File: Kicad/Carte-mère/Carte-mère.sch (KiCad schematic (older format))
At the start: 15 parts, among them P1 CONN_01X10, P2 CONN_01X04, P3 CONN_01X06, P4 CONN_01X06, P5 CONN_01X04, P6 CONN_01X04

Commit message: Mise à jour de la carte mère
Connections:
- net GND: now also ARD1.19 (GND), DRV1.15 (GND), DRV2.15 (GND)
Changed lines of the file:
@@
 Text Notes 5050 6350 0    60   ~ 0
 TX/RX communication
+$Comp
+L GND #PWR?
+U 1 1 55F57DDC
+P 5500 4700
+F 0 "#PWR?" H 5500 4700 30  0001 C CNN
+F 1 "GND" H 5500 4630 30  0001 C CNN
+F 2 "" H 5500 4700 60  0000 C CNN
+F 3 "" H 5500 4700 60  0000 C CNN
+	1    5500 4700
+	0    -1   -1   0
+$EndComp
+Wire Wire Line
+	5200 4700 5500 4700
+$Comp
+L GND #PWR?
+U 1 1 55F57EFC
+P 7950 4600
+F 0 "#PWR?" H 7950 4600 30  0001 C CNN
+F 1 "GND" H 7950 4530 30  0001 C CNN
+F 2 "" H 7950 4600 60  0000 C CNN
+F 3 "" H 7950 4600 60  0000 C CNN
+	1    7950 4600
+	0    -1   -1   0
+$EndComp
+Wire Wire Line
+	7750 4600 7950 4600
+$Comp
+L GND #PWR?
+U 1 1 55F57FF0
+P 7950 3550
+F 0 "#PWR?" H 7950 3550 30  0001 C CNN
+F 1 "GND" H 7950 3480 30  0001 C CNN
+F 2 "" H 7950 3550 60  0000 C CNN
+F 3 "" H 7950 3550 60  0000 C CNN
+	1    7950 3550
+	0    -1   -1   0
+$EndComp
+Wire Wire Line
+	7750 3550 7950 3550
 $EndSCHEMATC

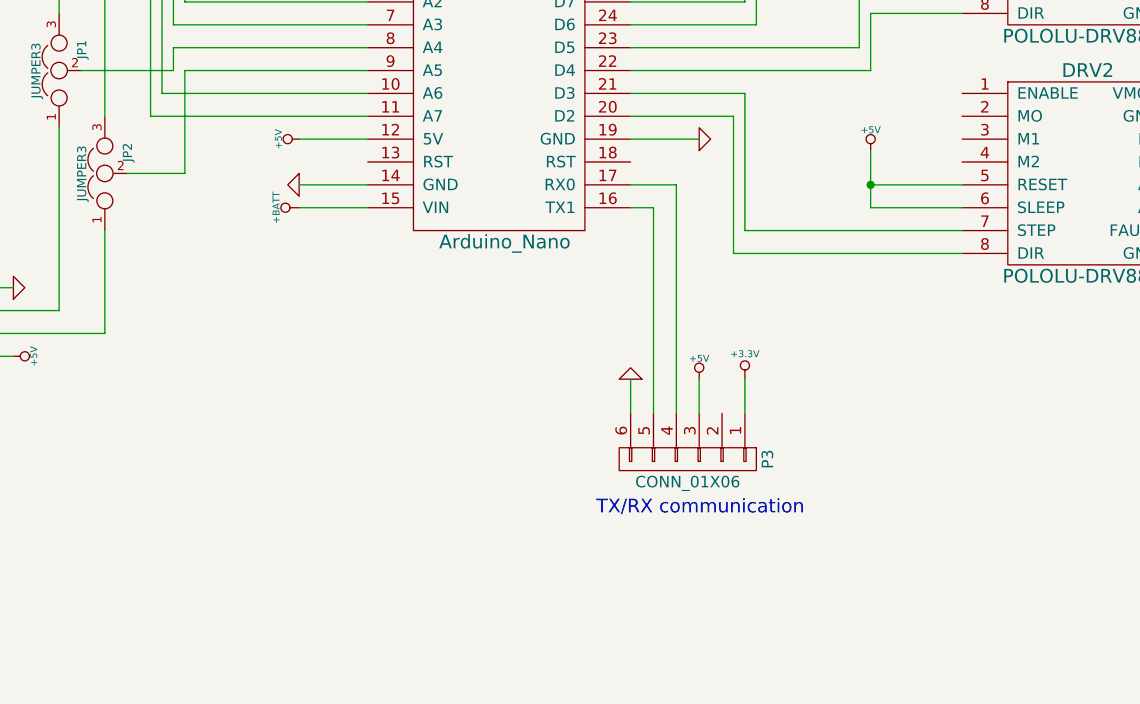
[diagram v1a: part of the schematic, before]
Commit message: Modification PCB pour prendre en compte les remarques faites à l'IUT
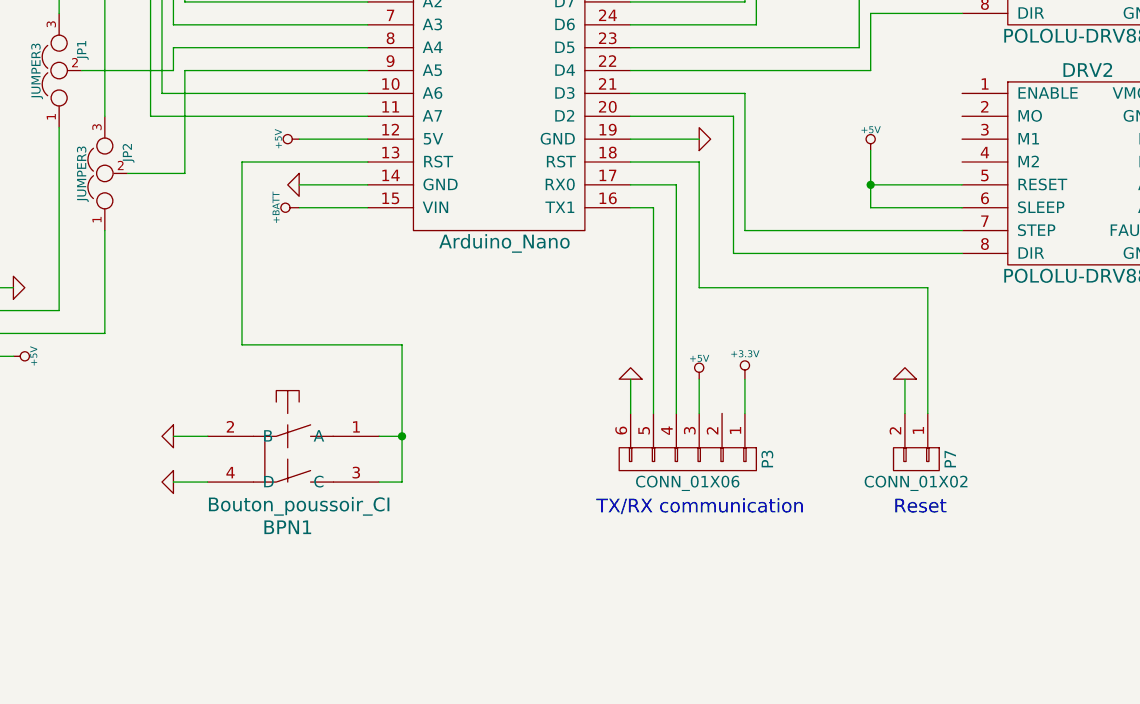
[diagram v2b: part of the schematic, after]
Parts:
- added BPN1: Bouton_poussoir_CI, Boutons:BPN-CI, symbol Bouton_poussoir_CI
- added P7: CONN_01X02, Pin_Headers:Pin_Header_Straight_1x02, symbol CONN_01X02
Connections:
- net GND: now also BPN1.2 (B), BPN1.4 (D), P7.2 (P2)
- net at ARD1.13 (RST): now also BPN1.1 (A), BPN1.3 (C)
- net at ARD1.18 (RST): now also P7.1 (P1)
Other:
- note added: "Reset"
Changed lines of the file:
@@
 EESchema Schematic File Version 2
+LIBS:Carte-mère-cache
+LIBS:74xgxx
+LIBS:74xx
+LIBS:ac-dc
+LIBS:actel
+LIBS:adc-dac
+LIBS:analog_switches
+LIBS:atmel
+LIBS:audio
+LIBS:brooktre
+LIBS:cmos4000
+LIBS:cmos_ieee
+LIBS:conn
+LIBS:contrib
+LIBS:cypress
+LIBS:dc-dc
+LIBS:device
+LIBS:digital-audio
+LIBS:display
+LIBS:dsp
+LIBS:elec-unifil
+LIBS:ftdi
+LIBS:gennum
+LIBS:graphic
+LIBS:hc11
+LIBS:intel
+LIBS:interface
+LIBS:ir
+LIBS:linear
+LIBS:logo
+LIBS:memory
+LIBS:microchip
+LIBS:microchip1
+LIBS:microchip_pic10mcu
+LIBS:microchip_pic12mcu
+LIBS:microchip_pic16mcu
+LIBS:microchip_pic18mcu
+LIBS:microcontrollers
+LIBS:motorola
+LIBS:msp430
+LIBS:nxp_armmcu
+LIBS:opto
+LIBS:philips
 LIBS:power
-LIBS:Carte-mère-cache
+LIBS:powerint
+LIBS:pspice
+LIBS:references
+LIBS:regul
+LIBS:relays
+LIBS:rfcom
+LIBS:sensors
+LIBS:siliconi
+LIBS:special
+LIBS:stm8
+LIBS:stm32
+LIBS:supertex
+LIBS:texas
+LIBS:transf
+LIBS:transistors
+LIBS:ttl_ieee
+LIBS:valves
+LIBS:video
+LIBS:xilinx
+LIBS:Symbols_DCDC-ACDC-Converter_RevC_20Jul2012
+LIBS:Symbols_EN60617_13Mar2013
+LIBS:Symbols_EN60617-10_HF-Radio_DRAFT_12Sep2013
+LIBS:Symbols_ICs-Diskrete_RevD10
+LIBS:Symbols_ICs-Opto_RevB_16Sep2013
+LIBS:Symbols_Microcontroller_Philips-NXP_RevA_06Oct2013
+LIBS:SymbolsSimilarEN60617+oldDIN617-RevE8
+LIBS:Symbols_Socket-DIN41612_RevA
+LIBS:Symbols_Transformer-Diskrete_RevA
+LIBS:bouton_poussoir_ci
 EELAYER 25 0
 EELAYER END
@@
 TX/RX communication
 $Comp
-L GND #PWR?
+L GND #PWR025
 U 1 1 55F57DDC
 P 5500 4700
-F 0 "#PWR?" H 5500 4700 30  0001 C CNN
+F 0 "#PWR025" H 5500 4700 30  0001 C CNN
 F 1 "GND" H 5500 4630 30  0001 C CNN
 F 2 "" H 5500 4700 60  0000 C CNN
@@
 	5200 4700 5500 4700
 $Comp
-L GND #PWR?
+L GND #PWR026
 U 1 1 55F57EFC
 P 7950 4600
-F 0 "#PWR?" H 7950 4600 30  0001 C CNN
+F 0 "#PWR026" H 7950 4600 30  0001 C CNN
 F 1 "GND" H 7950 4530 30  0001 C CNN
 F 2 "" H 7950 4600 60  0000 C CNN
@@
 	7750 4600 7950 4600
 $Comp
-L GND #PWR?
+L GND #PWR027
 U 1 1 55F57FF0
 P 7950 3550
-F 0 "#PWR?" H 7950 3550 30  0001 C CNN
+F 0 "#PWR027" H 7950 3550 30  0001 C CNN
 F 1 "GND" H 7950 3480 30  0001 C CNN
 F 2 "" H 7950 3550 60  0000 C CNN
@@
 Wire Wire Line
 	7750 3550 7950 3550
+$Comp
+L CONN_01X02 P7
+U 1 1 55F71BCA
+P 6450 6100
+F 0 "P7" H 6450 6250 50  0000 C CNN
+F 1 "CONN_01X02" V 6550 6100 50  0000 C CNN
+F 2 "Pin_Headers:Pin_Header_Straight_1x02" H 6450 6100 60  0001 C CNN
+F 3 "" H 6450 6100 60  0000 C CNN
+	1    6450 6100
+	0    1    1    0
+$EndComp
+Text Notes 6350 6350 0    60   ~ 0
+Reset
+$Comp
+L Bouton_poussoir_CI BPN1
+U 1 1 55F72222
+P 3700 6100
+F 0 "BPN1" V 4000 6100 60  0000 C CNN
+F 1 "Bouton_poussoir_CI" V 3900 6150 60  0000 C CNN
+F 2 "Boutons:BPN-CI" H 3900 6100 60  0001 C CNN
+F 3 "" H 3900 6100 60  0000 C CNN
+	1    3700 6100
+	0    1    1    0
+$EndComp
+Wire Wire Line
+	4050 4800 3500 4800
+Wire Wire Line
+	3500 4800 3500 5600
+Wire Wire Line
+	3500 5600 4200 5600
+Wire Wire Line
+	4200 5600 4200 6200
+Wire Wire Line
+	4200 6000 4100 6000
+$Comp
+L GND #PWR028
+U 1 1 55F72580
+P 3200 6000
+F 0 "#PWR028" H 3200 6000 30  0001 C CNN
+F 1 "GND" H 3200 5930 30  0001 C CNN
+F 2 "" H 3200 6000 60  0000 C CNN
+F 3 "" H 3200 6000 60  0000 C CNN
+	1    3200 6000
+	0    1    1    0
+$EndComp
+$Comp
+L GND #PWR029
+U 1 1 55F725A5
+P 3200 6200
+F 0 "#PWR029" H 3200 6200 30  0001 C CNN
+F 1 "GND" H 3200 6130 30  0001 C CNN
+F 2 "" H 3200 6200 60  0000 C CNN
+F 3 "" H 3200 6200 60  0000 C CNN
+	1    3200 6200
+	0    1    1    0
+$EndComp
+Wire Wire Line
+	4200 6200 4100 6200
+Connection ~ 4200 6000
+Wire Wire Line
+	3350 6000 3200 6000
+Wire Wire Line
+	3350 6200 3200 6200
+$Comp
+L GND #PWR030
+U 1 1 55F727CC
+P 6400 5750
+F 0 "#PWR030" H 6400 5750 30  0001 C CNN
+F 1 "GND" H 6400 5680 30  0001 C CNN
+F 2 "" H 6400 5750 60  0000 C CNN
+F 3 "" H 6400 5750 60  0000 C CNN
+	1    6400 5750
+	-1   0    0    1
+$EndComp
+Wire Wire Line
+	6400 5750 6400 5900
+Wire Wire Line
+	6500 5900 6500 5350
+Wire Wire Line
+	6500 5350 5500 5350
+Wire Wire Line
+	5500 5350 5500 4800
+Wire Wire Line
+	5500 4800 5200 4800
 $EndSCHEMATC

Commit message: Ajout de la refonte de la carte mère
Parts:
- removed JP1, JP2: JUMPER3, Pin_Headers:Pin_Header_Straight_1x03, symbol JUMPER3
- removed P1: CONN_01X10, Pin_Headers:Pin_Header_Straight_1x10, symbol CONN_01X10
- added P1: CONN_01X08, Pin_Headers:Pin_Header_Straight_1x08, symbol CONN_01X08
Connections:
- net +5V: now also P1.8 (P8)
- net GND: now also P3.2 (P2), P1.1 (P1)
- net at ARD1.10 (A6): now also P1.3 (P3)
- net at ARD1.11 (A7): now also P1.2 (P2)
- net at ARD1.13 (RST), BPN1.1 (A), BPN1.3 (C): now also P7.1 (P1)
- net at ARD1.18 (RST): no longer P7.1 (P1)
- net at ARD1.4 (A0): now also P1.7 (P7)
- net at ARD1.5 (A1): now also P1.6 (P6)
- net at ARD1.6 (A2): now also P1.5 (P5)
- net at ARD1.7 (A3): now also P1.4 (P4)
- net at ARD1.8 (A4): now also P2.3 (P3)
- net at ARD1.9 (A5): now also P2.2 (P2)
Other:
- note removed: "A4"
- note removed: "A5"
- moved on the sheet: P7
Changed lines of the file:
@@
 A3
 Text Notes 1850 3500 0    60   ~ 0
-A4
+A6
 Text Notes 1850 3600 0    60   ~ 0
-A5
-Text Notes 1850 3700 0    60   ~ 0
-A6
-Text Notes 1850 3800 0    60   ~ 0
 A7
-$Comp
-L CONN_01X10 P1
-U 1 1 55F4A5C3
-P 2100 3400
-F 0 "P1" H 2100 3950 50  0000 C CNN
-F 1 "CONN_01X10" V 2200 3400 50  0000 C CNN
-F 2 "Pin_Headers:Pin_Header_Straight_1x10" H 2100 3400 60  0001 C CNN
-F 3 "" H 2100 3400 60  0000 C CNN
-	1    2100 3400
-	-1   0    0    1
-$EndComp
 Text Notes 1850 3000 0    60   ~ 0
 GND
-Text Notes 1800 3900 0    60   ~ 0
+Text Notes 1800 3700 0    60   ~ 0
 +5V
 Wire Wire Line
@@
 Wire Wire Line
 	3200 4200 4050 4200
-$Comp
-L JUMPER3 JP1
-U 1 1 55F4A97B
-P 2700 4400
-F 0 "JP1" H 2750 4300 40  0000 L CNN
-F 1 "JUMPER3" H 2700 4500 40  0000 C CNN
-F 2 "Pin_Headers:Pin_Header_Straight_1x03" H 2700 4400 60  0001 C CNN
-F 3 "" H 2700 4400 60  0000 C CNN
-	1    2700 4400
-	0    -1   -1   0
-$EndComp
-$Comp
-L JUMPER3 JP2
-U 1 1 55F4AAAA
-P 2900 4850
-F 0 "JP2" H 2950 4750 40  0000 L CNN
-F 1 "JUMPER3" H 2900 4950 40  0000 C CNN
-F 2 "Pin_Headers:Pin_Header_Straight_1x03" H 2900 4850 60  0001 C CNN
-F 3 "" H 2900 4850 60  0000 C CNN
-	1    2900 4850
-	0    -1   -1   0
-$EndComp
-Wire Wire Line
-	2300 3450 2900 3450
-Wire Wire Line
-	2900 3450 2900 4600
-Wire Wire Line
-	2300 3550 2700 3550
-Wire Wire Line
-	2700 3550 2700 4150
-Wire Wire Line
-	2800 4400 3200 4400
-Wire Wire Line
-	3200 4400 3200 4300
-Wire Wire Line
-	3200 4300 4050 4300
-Wire Wire Line
-	3000 4850 3250 4850
-Wire Wire Line
-	3250 4850 3250 4400
-Wire Wire Line
-	3250 4400 4050 4400
-Wire Wire Line
-	2300 5450 2700 5450
-Wire Wire Line
-	2700 5450 2700 4650
-Wire Wire Line
-	2300 5550 2900 5550
-Wire Wire Line
-	2900 5550 2900 5100
-Wire Wire Line
-	2300 3650 3150 3650
-Wire Wire Line
-	3150 3650 3150 4500
+Wire Wire Line
+	2300 3450 3150 3450
+Wire Wire Line
+	3150 3450 3150 4500
 Wire Wire Line
 	3150 4500 4050 4500
@@
 	4050 4600 3100 4600
 Wire Wire Line
-	3100 4600 3100 3750
-Wire Wire Line
-	3100 3750 2300 3750
+	3100 4600 3100 3550
+Wire Wire Line
+	3100 3550 2300 3550
 $Comp
 L +5V #PWR016
@@
 L GND #PWR017
 U 1 1 55F4AF40
-P 2450 3850
-F 0 "#PWR017" H 2450 3850 30  0001 C CNN
-F 1 "GND" H 2450 3780 30  0001 C CNN
-F 2 "" H 2450 3850 60  0000 C CNN
-F 3 "" H 2450 3850 60  0000 C CNN
-	1    2450 3850
+P 2450 3650
+F 0 "#PWR017" H 2450 3650 30  0001 C CNN
+F 1 "GND" H 2450 3580 30  0001 C CNN
+F 2 "" H 2450 3650 60  0000 C CNN
+F 3 "" H 2450 3650 60  0000 C CNN
+	1    2450 3650
 	0    -1   -1   0
 $EndComp
@@
 	2450 2950 2300 2950
 Wire Wire Line
-	2450 3850 2300 3850
+	2450 3650 2300 3650
 Wire Wire Line
 	5200 5000 5300 5000
@@
 L CONN_01X02 P7
 U 1 1 55F71BCA
-P 6450 6100
-F 0 "P7" H 6450 6250 50  0000 C CNN
-F 1 "CONN_01X02" V 6550 6100 50  0000 C CNN
-F 2 "Pin_Headers:Pin_Header_Straight_1x02" H 6450 6100 60  0001 C CNN
-F 3 "" H 6450 6100 60  0000 C CNN
-	1    6450 6100
-	0    1    1    0
-$EndComp
-Text Notes 6350 6350 0    60   ~ 0
+P 4650 6100
+F 0 "P7" H 4650 6250 50  0000 C CNN
+F 1 "CONN_01X02" V 4750 6100 50  0000 C CNN
+F 2 "Pin_Headers:Pin_Header_Straight_1x02" H 4650 6100 60  0001 C CNN
+F 3 "" H 4650 6100 60  0000 C CNN
+	1    4650 6100
+	0    1    1    0
+$EndComp
+Text Notes 4550 6350 0    60   ~ 0
 Reset
 $Comp
@@
 	3500 5600 4200 5600
 Wire Wire Line
-	4200 5600 4200 6200
+	4200 5350 4200 6200
 Wire Wire Line
 	4200 6000 4100 6000
@@
 L GND #PWR030
 U 1 1 55F727CC
-P 6400 5750
-F 0 "#PWR030" H 6400 5750 30  0001 C CNN
-F 1 "GND" H 6400 5680 30  0001 C CNN
-F 2 "" H 6400 5750 60  0000 C CNN
-F 3 "" H 6400 5750 60  0000 C CNN
-	1    6400 5750
+P 4600 5750
+F 0 "#PWR030" H 4600 5750 30  0001 C CNN
+F 1 "GND" H 4600 5680 30  0001 C CNN
+F 2 "" H 4600 5750 60  0000 C CNN
+F 3 "" H 4600 5750 60  0000 C CNN
+	1    4600 5750
 	-1   0    0    1
 $EndComp
 Wire Wire Line
-	6400 5750 6400 5900
-Wire Wire Line
-	6500 5900 6500 5350
-Wire Wire Line
-	6500 5350 5500 5350
-Wire Wire Line
-	5500 5350 5500 4800
-Wire Wire Line
-	5500 4800 5200 4800
+	4600 5750 4600 5900
+Wire Wire Line
+	4700 5900 4700 5350
+$Comp
+L CONN_01X08 P1
+U 1 1 55FDC168
+P 2100 3300
+F 0 "P1" H 2100 3750 50  0000 C CNN
+F 1 "CONN_01X08" V 2200 3300 50  0000 C CNN
+F 2 "Pin_Headers:Pin_Header_Straight_1x08" H 2100 3300 60  0001 C CNN
+F 3 "" H 2100 3300 60  0000 C CNN
+	1    2100 3300
+	-1   0    0    1
+$EndComp
+Connection ~ 4200 5600
+Wire Wire Line
+	4700 5350 4200 5350
+$Comp
+L GND #PWR031
+U 1 1 55FDEAA3
+P 5600 5750
+F 0 "#PWR031" H 5600 5750 30  0001 C CNN
+F 1 "GND" H 5600 5680 30  0001 C CNN
+F 2 "" H 5600 5750 60  0000 C CNN
+F 3 "" H 5600 5750 60  0000 C CNN
+	1    5600 5750
+	-1   0    0    1
+$EndComp
+Wire Wire Line
+	5600 5750 5600 5900
+Wire Wire Line
+	4050 4300 2700 4300
+Wire Wire Line
+	2700 4300 2700 5450
+Wire Wire Line
+	2700 5450 2300 5450
+Wire Wire Line
+	2300 5550 2750 5550
+Wire Wire Line
+	2750 5550 2750 4400
+Wire Wire Line
+	2750 4400 4050 4400
 $EndSCHEMATC

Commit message: Mise à jour de la carte mère
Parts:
- added P10, P11, P8, P9: CONN_01X04, Pin_Headers:Pin_Header_Straight_1x04, symbol CONN_01X04
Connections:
- net +5V: now also P10.1 (P1), P10.2 (P2), P10.3 (P3), P10.4 (P4), P8.1 (P1), P8.2 (P2), P8.3 (P3), P8.4 (P4)
- net GND: now also P11.1 (P1), P11.2 (P2), P11.3 (P3), P11.4 (P4), P9.1 (P1), P9.2 (P2), P9.3 (P3), P9.4 (P4)
